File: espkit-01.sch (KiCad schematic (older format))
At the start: 14 parts, among them IC1 WS2812B, P1 ESP-01, P2 BREAKOUT, P3 SERIAL, P4 PWR, P5 NEOPIXEL, P6 BRIDGE, SW1 RESET, SW2 PRGM

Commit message: Added single layer version
or, at least, as single as possible.  There are 4 connections on the
back, but they are between pins.
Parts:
- C3: value 10uf -> 1uf
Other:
- moved on the sheet: P2, P4
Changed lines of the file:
@@
 LIBS:contrib
 LIBS:valves
-LIBS:trinkle-cache
-LIBS:isolinear_reader
-LIBS:mages_mega
-LIBS:ESP-01-Breakout-cache
+LIBS:espkit-01-cache
 EELAYER 27 0
 EELAYER END
@@
 Sheet 1 1
 Title ""
-Date "26 feb 2015"
+Date "4 mar 2015"
 Rev ""
 Comp ""
@@
 L CONN_2 P2
 U 1 1 54EDD989
-P 1300 2400
-F 0 "P2" V 1250 2400 40  0000 C CNN
-F 1 "BREAKOUT" V 1350 2400 40  0000 C CNN
-F 2 "" H 1300 2400 60  0000 C CNN
-F 3 "" H 1300 2400 60  0000 C CNN
-	1    1300 2400
+P 1250 2450
+F 0 "P2" V 1200 2450 40  0000 C CNN
+F 1 "BREAKOUT" V 1300 2450 40  0000 C CNN
+F 2 "" H 1250 2450 60  0000 C CNN
+F 3 "" H 1250 2450 60  0000 C CNN
+	1    1250 2450
 	1    0    0    -1
 $EndComp
@@
 Text GLabel 1700 1950 2    60   Input ~ 0
 GPIO2
-Text GLabel 950  2300 0    60   Input ~ 0
+Text GLabel 900  2350 0    60   Input ~ 0
 GPIO0
-Text GLabel 950  2500 0    60   Input ~ 0
+Text GLabel 900  2550 0    60   Input ~ 0
 GPIO2
 $Comp
@@
 P 4000 2050
 F 0 "C3" H 4000 2150 40  0000 L CNN
-F 1 "10uf" H 4006 1965 40  0000 L CNN
+F 1 "1uf" H 4006 1965 40  0000 L CNN
 F 2 "~" H 4038 1900 30  0000 C CNN
 F 3 "~" H 4000 2050 60  0000 C CNN
@@
 L CONN_2 P4
 U 1 1 54EDDD55
-P 2050 2400
-F 0 "P4" V 2000 2400 40  0000 C CNN
-F 1 "PWR" V 2100 2400 40  0000 C CNN
-F 2 "" H 2050 2400 60  0000 C CNN
-F 3 "" H 2050 2400 60  0000 C CNN
-	1    2050 2400
+P 2050 2450
+F 0 "P4" V 2000 2450 40  0000 C CNN
+F 1 "PWR" V 2100 2450 40  0000 C CNN
+F 2 "" H 2050 2450 60  0000 C CNN
+F 3 "" H 2050 2450 60  0000 C CNN
+	1    2050 2450
 	1    0    0    -1
 $EndComp
@@
 L GND #PWR7
 U 1 1 54EDDD5B
-P 1700 2500
-F 0 "#PWR7" H 1700 2500 30  0001 C CNN
-F 1 "GND" H 1700 2430 30  0001 C CNN
-F 2 "" H 1700 2500 60  0000 C CNN
-F 3 "" H 1700 2500 60  0000 C CNN
-	1    1700 2500
+P 1700 2550
+F 0 "#PWR7" H 1700 2550 30  0001 C CNN
+F 1 "GND" H 1700 2480 30  0001 C CNN
+F 2 "" H 1700 2550 60  0000 C CNN
+F 3 "" H 1700 2550 60  0000 C CNN
+	1    1700 2550
 	0    1    1    0
 $EndComp
@@
 L +3.3V #PWR6
 U 1 1 54EDDD61
-P 1700 2300
-F 0 "#PWR6" H 1700 2260 30  0001 C CNN
-F 1 "+3.3V" H 1700 2410 30  0000 C CNN
-F 2 "" H 1700 2300 60  0000 C CNN
-F 3 "" H 1700 2300 60  0000 C CNN
-	1    1700 2300
-	0    -1   -1   0
-$EndComp
+P 1700 2350
+F 0 "#PWR6" H 1700 2310 30  0001 C CNN
+F 1 "+3.3V" H 1700 2460 30  0000 C CNN
+F 2 "" H 1700 2350 60  0000 C CNN
+F 3 "" H 1700 2350 60  0000 C CNN
+	1    1700 2350
+	0    -1   -1   0
+$EndComp

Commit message: Shuffled Layout for 1.1
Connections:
- wire segments 15 -> 14
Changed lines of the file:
@@
 LIBS:contrib
 LIBS:valves
+LIBS:mages_mega
 LIBS:espkit-01-cache
 EELAYER 27 0
@@
 Sheet 1 1
 Title ""
-Date "4 mar 2015"
+Date "13 mar 2015"
 Rev ""
 Comp ""
@@
 $EndComp
 $Comp
-L GND #PWR17
+L GND #PWR18
 U 1 1 54EDD68F
 P 3850 650
-F 0 "#PWR17" H 3850 650 30  0001 C CNN
+F 0 "#PWR18" H 3850 650 30  0001 C CNN
 F 1 "GND" H 3850 580 30  0001 C CNN
 F 2 "" H 3850 650 60  0000 C CNN
@@
 $EndComp
 $Comp
-L +3.3V #PWR18
+L +3.3V #PWR19
 U 1 1 54EDD6B7
 P 3850 850
-F 0 "#PWR18" H 3850 810 30  0001 C CNN
+F 0 "#PWR19" H 3850 810 30  0001 C CNN
 F 1 "+3.3V" H 3850 960 30  0000 C CNN
 F 2 "" H 3850 850 60  0000 C CNN
@@
 Wire Wire Line
 	3850 1050 3800 1050
+Text GLabel 1500 1050 0    60   Input ~ 0
+TX
 Text GLabel 2500 1350 2    60   Input ~ 0
-TX
-Text GLabel 1500 1050 0    60   Input ~ 0
 RX
 Wire Wire Line
@@
 	2850 2450 2650 2450
 $Comp
-L +3.3V #PWR19
+L +3.3V #PWR20
 U 1 1 54EDDC41
 P 4300 1850
-F 0 "#PWR19" H 4300 1810 30  0001 C CNN
+F 0 "#PWR20" H 4300 1810 30  0001 C CNN
 F 1 "+3.3V" H 4300 1960 30  0000 C CNN
 F 2 "" H 4300 1850 60  0000 C CNN
@@
 $EndComp
 $Comp
-L GND #PWR16
+L GND #PWR17
 U 1 1 54EDDC5F
 P 3500 1850
-F 0 "#PWR16" H 3500 1850 30  0001 C CNN
+F 0 "#PWR17" H 3500 1850 30  0001 C CNN
 F 1 "GND" H 3500 1780 30  0001 C CNN
 F 2 "" H 3500 1850 60  0000 C CNN
@@
 $EndComp
 $Comp
-L GND #PWR7
+L GND #PWR6
 U 1 1 54EDDD5B
+P 1700 2350
+F 0 "#PWR6" H 1700 2350 30  0001 C CNN
+F 1 "GND" H 1700 2280 30  0001 C CNN
+F 2 "" H 1700 2350 60  0000 C CNN
+F 3 "" H 1700 2350 60  0000 C CNN
+	1    1700 2350
+	0    1    1    0
+$EndComp
+$Comp
+L +3.3V #PWR7
+U 1 1 54EDDD61
 P 1700 2550
-F 0 "#PWR7" H 1700 2550 30  0001 C CNN
-F 1 "GND" H 1700 2480 30  0001 C CNN
+F 0 "#PWR7" H 1700 2510 30  0001 C CNN
+F 1 "+3.3V" H 1700 2660 30  0000 C CNN
 F 2 "" H 1700 2550 60  0000 C CNN
 F 3 "" H 1700 2550 60  0000 C CNN
 	1    1700 2550
-	0    1    1    0
-$EndComp
-$Comp
-L +3.3V #PWR6
-U 1 1 54EDDD61
-P 1700 2350
-F 0 "#PWR6" H 1700 2310 30  0001 C CNN
-F 1 "+3.3V" H 1700 2460 30  0000 C CNN
-F 2 "" H 1700 2350 60  0000 C CNN
-F 3 "" H 1700 2350 60  0000 C CNN
-	1    1700 2350
 	0    -1   -1   0
 $EndComp
@@
 	0    -1   -1   0
 $EndComp
-Wire Wire Line
-	1500 1950 1700 1950
 Connection ~ 1700 1950
 Connection ~ 1500 1950

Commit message: Redundant power led removed
bridge connection now easy to get too.
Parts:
- removed D1: PWR_LED, ~, symbol LED
- removed R3: 1K, ~, symbol R
- IC1: Cost per unit (quantity 100) (none) -> 0.08
- P1: Cost per unit (quantity 100) (none) -> 0.05
- SW1, SW2: Cost per unit (quantity 100) (none) -> 0.06
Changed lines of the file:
@@
 Sheet 1 1
 Title ""
-Date "13 mar 2015"
+Date "29 may 2015"
 Rev ""
 Comp ""
@@
 F 2 "~" H 2450 1650 60  0000 C CNN
 F 3 "~" H 2450 1650 60  0000 C CNN
+F 4 "0.06" H 2450 1650 60  0001 C CNN "Cost per unit (quantity 100)"
 	1    2450 1650
 	1    0    0    -1
@@
 F 2 "~" H 1100 2000 60  0000 C CNN
 F 3 "~" H 1100 2000 60  0000 C CNN
+F 4 "0.08" H 1100 2000 60  0001 C CNN "Cost per unit (quantity 100)"
 	1    1100 2000
 	1    0    0    -1
@@
 F 2 "~" H 2850 1150 60  0000 C CNN
 F 3 "~" H 2850 1150 60  0000 C CNN
+F 4 "0.06" H 2850 1150 60  0001 C CNN "Cost per unit (quantity 100)"
 	1    2850 1150
 	1    0    0    -1
@@
 Connection ~ 3800 1850
 $Comp
-L +3.3V #PWR5
-U 1 1 54EDDD05
-P 1550 700
-F 0 "#PWR5" H 1550 660 30  0001 C CNN
-F 1 "+3.3V" H 1550 810 30  0000 C CNN
-F 2 "" H 1550 700 60  0000 C CNN
-F 3 "" H 1550 700 60  0000 C CNN
-	1    1550 700
-	0    1    1    0
-$EndComp
-$Comp
-L GND #PWR1
-U 1 1 54EDDD0B
-P 650 700
-F 0 "#PWR1" H 650 700 30  0001 C CNN
-F 1 "GND" H 650 630 30  0001 C CNN
-F 2 "" H 650 700 60  0000 C CNN
-F 3 "" H 650 700 60  0000 C CNN
-	1    650  700
-	0    1    1    0
-$EndComp
-$Comp
-L R R3
-U 1 1 54EDDD11
-P 1300 700
-F 0 "R3" V 1380 700 40  0000 C CNN
-F 1 "1K" V 1307 701 40  0000 C CNN
-F 2 "~" V 1230 700 30  0000 C CNN
-F 3 "~" H 1300 700 30  0000 C CNN
-	1    1300 700
-	0    -1   -1   0
-$EndComp
-$Comp
-L LED D1
-U 1 1 54EDDD2D
-P 850 700
-F 0 "D1" H 850 800 50  0000 C CNN
-F 1 "PWR_LED" H 850 600 50  0000 C CNN
-F 2 "~" H 850 700 60  0000 C CNN
-F 3 "~" H 850 700 60  0000 C CNN
-	1    850  700
-	-1   0    0    1
-$EndComp
-$Comp
 L CONN_2 P4
 U 1 1 54EDDD55
@@
 F 2 "" H 1900 1200 60  0000 C CNN
 F 3 "" H 1900 1200 60  0000 C CNN
+F 4 "0.05" H 1900 1200 60  0001 C CNN "Cost per unit (quantity 100)"
 	1    1900 1200
 	1    0    0    -1

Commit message: New Design with auto program.
You should be able to do away with the serial/usb programmer and just use the NodeMCU v1.0 board in Arduino to auto-program.
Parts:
- removed C2: 0.1uf, ~, symbol C
- removed C3: 1uf, ~, symbol C
- removed P3: SERIAL, symbol CONN_6
- added C1, C6: 10uF, Capacitors_SMD:C_0603_HandSoldering, symbol C
- added C4, C7: 0.1uF, Capacitors_SMD:C_0603_HandSoldering, symbol C
- added C5: 1uF, Capacitors_SMD:C_0603_HandSoldering, symbol C
- added C8: 10uF 6.3V A TANT, Capacitors_SMD:C_0603_HandSoldering, symbol CP1
- added P3: USB_5PIN_SHELL, freetronics_footprints:USB-MICRO-5pin_PTHMOUNT, symbol USB_5PIN_SHELL
- added Q1, Q2: S8050, TO_SOT_Packages_SMD:SOT-23_Handsoldering, symbol S8050
- added R2, R3: 12K(1%), Resistors_SMD:R_0603_HandSoldering, symbol R
- added R4: 10K, Resistors_SMD:R_0603_HandSoldering, symbol R
- added R5: 470R(1%), Resistors_SMD:R_0603_HandSoldering, symbol R
- added U1: LD1117, TO_SOT_Packages_SMD:SOT-223, symbol LD1117
- added U2: CP2102, Housings_DFN_QFN:QFN-28-1EP_5x5mm_Pitch0.5mm, symbol CP2102
- IC1: footprint ~ -> libs:ws2812b; symbol WS2812B -> WS2812b
- P1: footprint (none) -> Pin_Headers:Pin_Header_Straight_2x04
- P2, P4: footprint (none) -> Pin_Headers:Pin_Header_Straight_1x02
- P5: footprint (none) -> Pin_Headers:Pin_Header_Straight_1x04
- P6: footprint (none) -> libs:603_bridge
- R1: footprint ~ -> Resistors_SMD:R_0603_HandSoldering
- SW1, SW2: footprint ~ -> libs:1107G
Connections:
- net labels added: +5V, 3.3, 5, CTS, DCD, DSR, DTR, ESP_EN, RESET, RI, RTS, RXD, TXD, USB_D+, USB_D-
- net labels removed: RX, TX
- wire segments 14 -> 100
- no-connect marks 3 -> 5
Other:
- moved on the sheet: P1, P2, P4, P5, P6, SW1, SW2

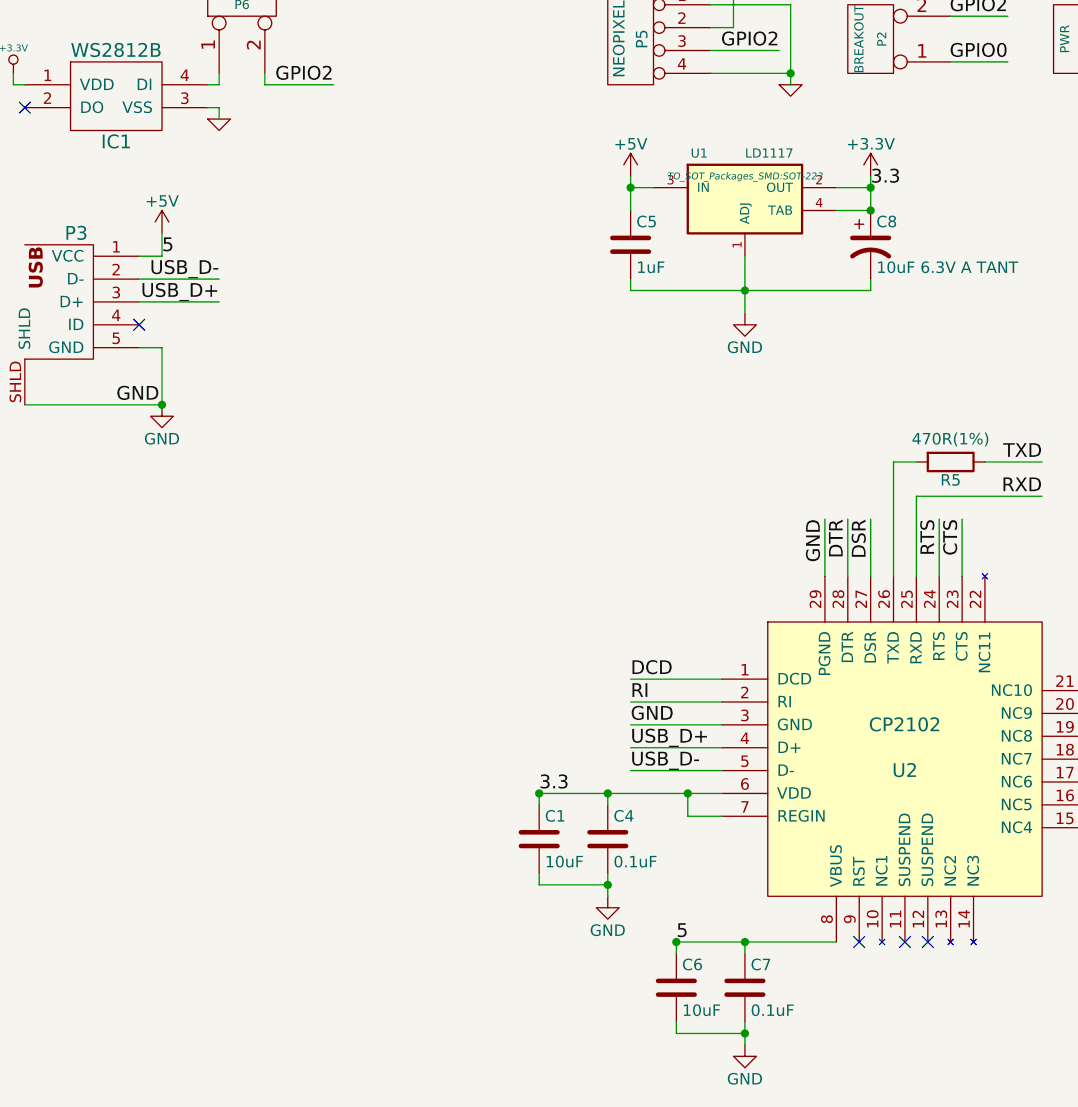
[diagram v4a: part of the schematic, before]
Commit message: Sometimes helps to connect your grounds.
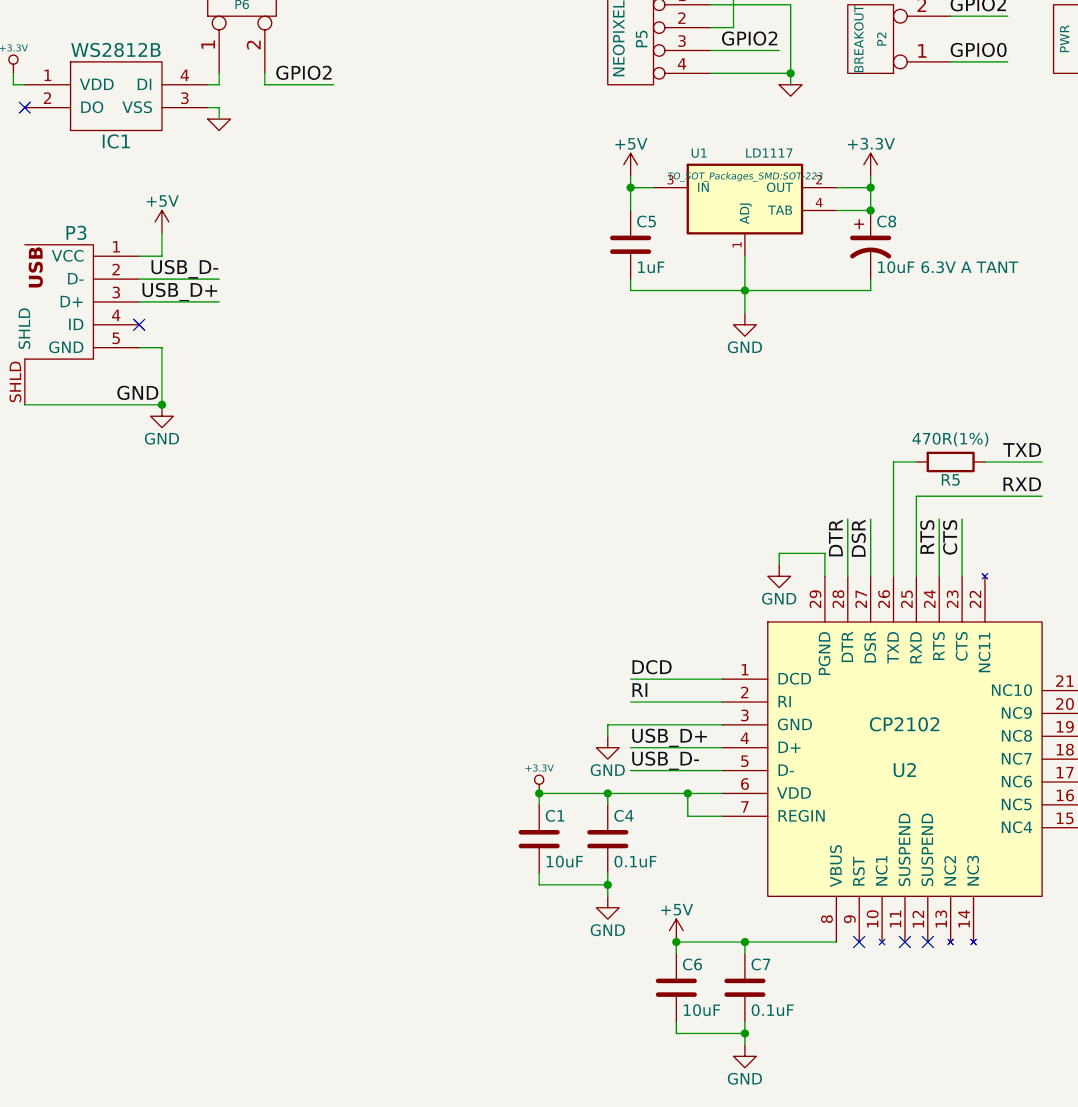
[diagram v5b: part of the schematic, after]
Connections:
- net +3.3V: now also C1.1, C4.1, U2.6 (VDD), U2.7 (REGIN)
- net +3V3: no longer C1.1, C4.1, U2.6 (VDD), U2.7 (REGIN)
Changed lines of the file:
@@
 $EndComp
 Wire Wire Line
-	4200 4100 4200 3850
-Text Label 4200 3850 3    60   ~ 0
-GND
-Wire Wire Line
-	3750 4750 3350 4750
-Text Label 3350 4750 0    60   ~ 0
-GND
-Wire Wire Line
 	2950 5100 2950 5050
-Text Label 2950 5050 0    60   ~ 0
-3.3
 Wire Wire Line
 	3550 5750 3550 5700
-Text Label 3550 5700 0    60   ~ 0
-5
-Text Label 4400 2400 0    60   ~ 0
-3.3
-Text Label 1300 2700 0    60   ~ 0
-5
 Text Label 1100 3350 0    60   ~ 0
 GND
+$Comp
+L +5V #PWR?
+U 1 1 580DC2F8
+P 3550 5700
+F 0 "#PWR?" H 3550 5550 50  0001 C CNN
+F 1 "+5V" H 3550 5840 50  0000 C CNN
+F 2 "" H 3550 5700 50  0000 C CNN
+F 3 "" H 3550 5700 50  0000 C CNN
+	1    3550 5700
+	1    0    0    -1
+$EndComp
+$Comp
+L +3.3V-RESCUE-espkit-01 #PWR?
+U 1 1 580DC5A3
+P 2950 5050
+F 0 "#PWR?" H 2950 5010 30  0001 C CNN
+F 1 "+3.3V" H 2950 5160 30  0000 C CNN
+F 2 "" H 2950 5050 60  0000 C CNN
+F 3 "" H 2950 5050 60  0000 C CNN
+	1    2950 5050
+	1    0    0    -1
+$EndComp
+$Comp
+L GND #PWR?
+U 1 1 580DD86E
+P 3250 4800
+F 0 "#PWR?" H 3250 4550 50  0001 C CNN
+F 1 "GND" H 3250 4650 50  0000 C CNN
+F 2 "" H 3250 4800 50  0000 C CNN
+F 3 "" H 3250 4800 50  0000 C CNN
+	1    3250 4800
+	1    0    0    -1
+$EndComp
+$Comp
+L GND #PWR?
+U 1 1 580DD8C1
+P 4000 4050
+F 0 "#PWR?" H 4000 3800 50  0001 C CNN
+F 1 "GND" H 4000 3900 50  0000 C CNN
+F 2 "" H 4000 4050 50  0000 C CNN
+F 3 "" H 4000 4050 50  0000 C CNN
+	1    4000 4050
+	1    0    0    -1
+$EndComp
+Wire Wire Line
+	4200 4100 4200 4000
+Wire Wire Line
+	4200 4000 4000 4000
+Wire Wire Line
+	4000 4000 4000 4050
+Wire Wire Line
+	3250 4750 3750 4750
+Wire Wire Line
+	3250 4750 3250 4800
 $EndSCHEMATC
